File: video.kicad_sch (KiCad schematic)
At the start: 48 parts, among them IC108 μPC358C, IC903 HUC6260, Q902 25C945, Q903 25A733, Q904 25C945

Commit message: IC routing mostly complete, start adding passives.
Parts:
- C101, C104, C105, C106, C107, C151: footprint Capacitor_SMD:C_0805_2012Metric -> A-PCENGINE:SMD_0805_Narrow
- R103, R104: footprint Resistor_SMD:R_0805_2012Metric -> A-PCENGINE:SMD_0805_Narrow

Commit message: Bunch of passives and what-not.
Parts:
- removed L102: ~, A-PCENGINE:L-5.00mm, symbol Device:L
- removed R103: 680, A-PCENGINE:SMD_0805_Narrow, symbol Device:R
- removed R103: 2.7K, A-PCENGINE:SMD_0805_Narrow, symbol Device:R
- C101, C107, R103, R104: footprint A-PCENGINE:SMD_0805_Narrow -> A-PCENGINE:SMD_0805_Narrow_Long
- R103: footprint Resistor_SMD:R_2010_5025Metric -> A-PCENGINE:SMD_2010
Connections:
- net at C101.1, Q904.3 (E), R103.1: no longer R103.2
- net at C101.2: now also R103.2
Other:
- moved on the sheet: C101, C107, C151, IC108A, R103, R104

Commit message: More passives, custom footprints, etc.
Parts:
- removed IC108: μPC358C, A-PCENGINE:DIP-8, symbol Amplifier_Operational:LM358
- C101: footprint A-PCENGINE:Elec_P5.00mm -> A-PCENGINE:Elec_P5.00mm_D10.5mm
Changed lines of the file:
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@@
         )
         (path "/c1c718c6-a427-431e-a18b-e46f94ae8e09/c78d7e8a-3e65-46f4-91f4-96eb31925bea"
-          (reference "R159") (unit 1)
+          (reference "Rx159") (unit 1)
         )
       )
@@
     )
   )
-  (symbol (lib_id "Amplifier_Operational:LM358") (at 298.45 191.77 0) (unit 1)
-    (in_bom yes) (on_board yes) (dnp no)
-    (property "Reference" "IC108" (at 300.99 196.85 0)
-      (effects (font (size 1.27 1.27)))
-    )
-    (property "Value" "μPC358C" (at 300.99 199.39 0)
-      (effects (font (size 1.27 1.27)))
-    )
-    (property "Footprint" "A-PCENGINE:DIP-8" (at 298.45 191.77 0)
-      (effects (font (size 1.27 1.27)) hide)
-    )
-    (property "Datasheet" "http://www.ti.com/lit/ds/symlink/lm2904-n.pdf" (at 298.45 191.77 0)
-      (effects (font (size 1.27 1.27)) hide)
-    )
-    (pin "1")
-    (pin "2")
-    (pin "3")
-    (pin "5")
-    (pin "6")
-    (pin "7")
-    (pin "4")
-    (pin "8")
-    (instances
-      (project "PCE"
-        (path "/c1c718c6-a427-431e-a18b-e46f94ae8e09/1d91d06a-381a-4a70-bfc1-2abf4d159a91"
-          (reference "IC108") (unit 1)
-        )
-        (path "/c1c718c6-a427-431e-a18b-e46f94ae8e09/c78d7e8a-3e65-46f4-91f4-96eb31925bea"
-          (reference "ICX108") (unit 1)
-        )
-      )
-    )
-  )
   (symbol (lib_id "Device:C_Polarized") (at 95.25 132.08 270) (unit 1)
     (in_bom yes) (on_board yes) (dnp no)
@@
         )
         (path "/c1c718c6-a427-431e-a18b-e46f94ae8e09/c78d7e8a-3e65-46f4-91f4-96eb31925bea"
-          (reference "R158") (unit 1)
+          (reference "Rx158") (unit 1)
         )
       )
@@
       (effects (font (size 1.27 1.27)))
     )
-    (property "Footprint" "A-PCENGINE:Elec_P5.00mm" (at 283.5148 96.52 0)
-      (effects (font (size 1.27 1.27)) hide)
-    )
+    (property "Footprint" "A-PCENGINE:Elec_P5.00mm_D10.5mm" (at 283.5148 96.52 0)
+      (effects (font (size 1.27 1.27)) hide)
+    )

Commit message: Top layer first draft.
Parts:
- C101: footprint Capacitor_SMD:CP_Elec_4x3 -> A-PCENGINE:CP_6x1.5mm
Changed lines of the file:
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@@
         )
         (path "/c1c718c6-a427-431e-a18b-e46f94ae8e09/c78d7e8a-3e65-46f4-91f4-96eb31925bea"
-          (reference "R162") (unit 1)
+          (reference "Rx162") (unit 1)
         )
       )
@@
         )
         (path "/c1c718c6-a427-431e-a18b-e46f94ae8e09/c78d7e8a-3e65-46f4-91f4-96eb31925bea"
-          (reference "C152") (unit 1)
+          (reference "Cx152") (unit 1)
         )
       )
@@
         )
         (path "/c1c718c6-a427-431e-a18b-e46f94ae8e09/c78d7e8a-3e65-46f4-91f4-96eb31925bea"
-          (reference "R160") (unit 1)
+          (reference "Rx160") (unit 1)
         )
       )
@@
         )
         (path "/c1c718c6-a427-431e-a18b-e46f94ae8e09/c78d7e8a-3e65-46f4-91f4-96eb31925bea"
-          (reference "C151") (unit 1)
+          (reference "Cx151") (unit 1)
         )
       )
@@
       (effects (font (size 1.27 1.27)))
     )
-    (property "Footprint" "Capacitor_SMD:CP_Elec_4x3" (at 102.87 139.3952 0)
-      (effects (font (size 1.27 1.27)) hide)
-    )
+    (property "Footprint" "A-PCENGINE:CP_6x1.5mm" (at 102.87 139.3952 0)
+      (effects (font (size 1.27 1.27)) hide)
+    )

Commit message: First draft complete.
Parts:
- removed C107: 220pF, A-PCENGINE:SMD_0805_Narrow_Long, symbol Device:C
- removed C151: 15000pF, A-PCENGINE:SMD_0805_Narrow, symbol Device:C
- removed R104: 10K, A-PCENGINE:SMD_0805_Narrow, symbol Device:R
- removed R104: 5.1K, A-PCENGINE:SMD_0805_Narrow, symbol Device:R
- removed R104 (x3): 9.1K, A-PCENGINE:SMD_0805_Narrow, symbol Device:R
- removed R104: 1K, A-PCENGINE:SMD_0805_Narrow, symbol Device:R
- removed R104: 15K, A-PCENGINE:SMD_0805_Narrow, symbol Device:R

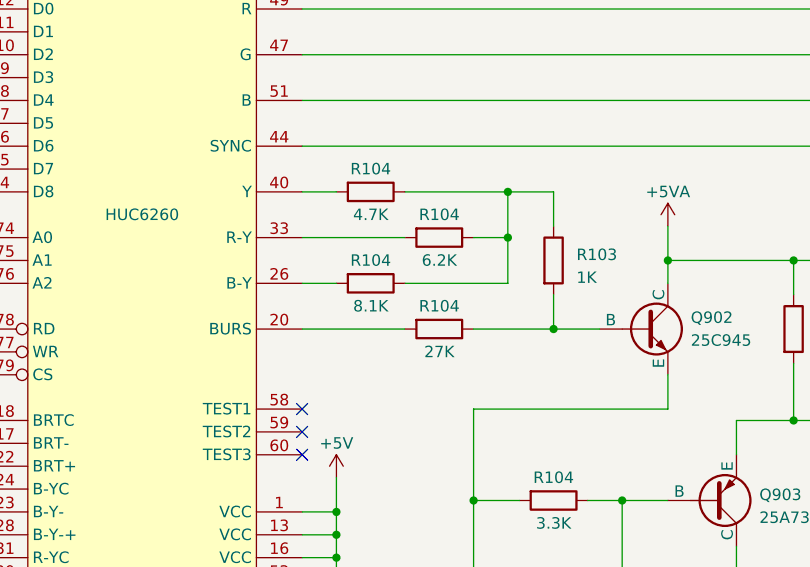
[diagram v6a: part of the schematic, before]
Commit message: Add resistor values to schematics.
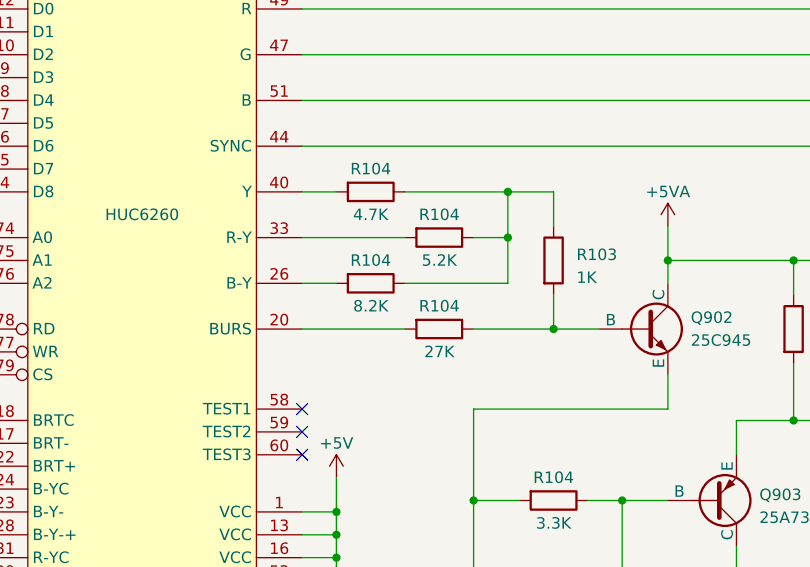
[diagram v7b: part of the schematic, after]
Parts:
- R104: value 6.2K -> 5.2K
- R104: value 8.1K -> 8.2K
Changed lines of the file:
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@@
       (effects (font (size 1.27 1.27)))
     )
-    (property "Value" "6.2K" (at 222.25 74.93 90)
+    (property "Value" "5.2K" (at 222.25 74.93 90)
       (effects (font (size 1.27 1.27)))
     )
@@
       (effects (font (size 1.27 1.27)))
     )
-    (property "Value" "8.1K" (at 214.63 80.01 90)
-      (effects (font (size 1.27 1.27)))
-    )
+    (property "Value" "8.2K" (at 214.63 80.01 90)
+      (effects (font (size 1.27 1.27)))
+    )
